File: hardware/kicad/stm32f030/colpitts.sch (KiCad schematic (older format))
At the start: 42 parts, among them P2 LOOP1, P3 LOOP2, Q1 BSS138, Q2 BC817-40, Q3 BSS138, Q4 BC817-40, T1 78601/9C, T2 78601/9C

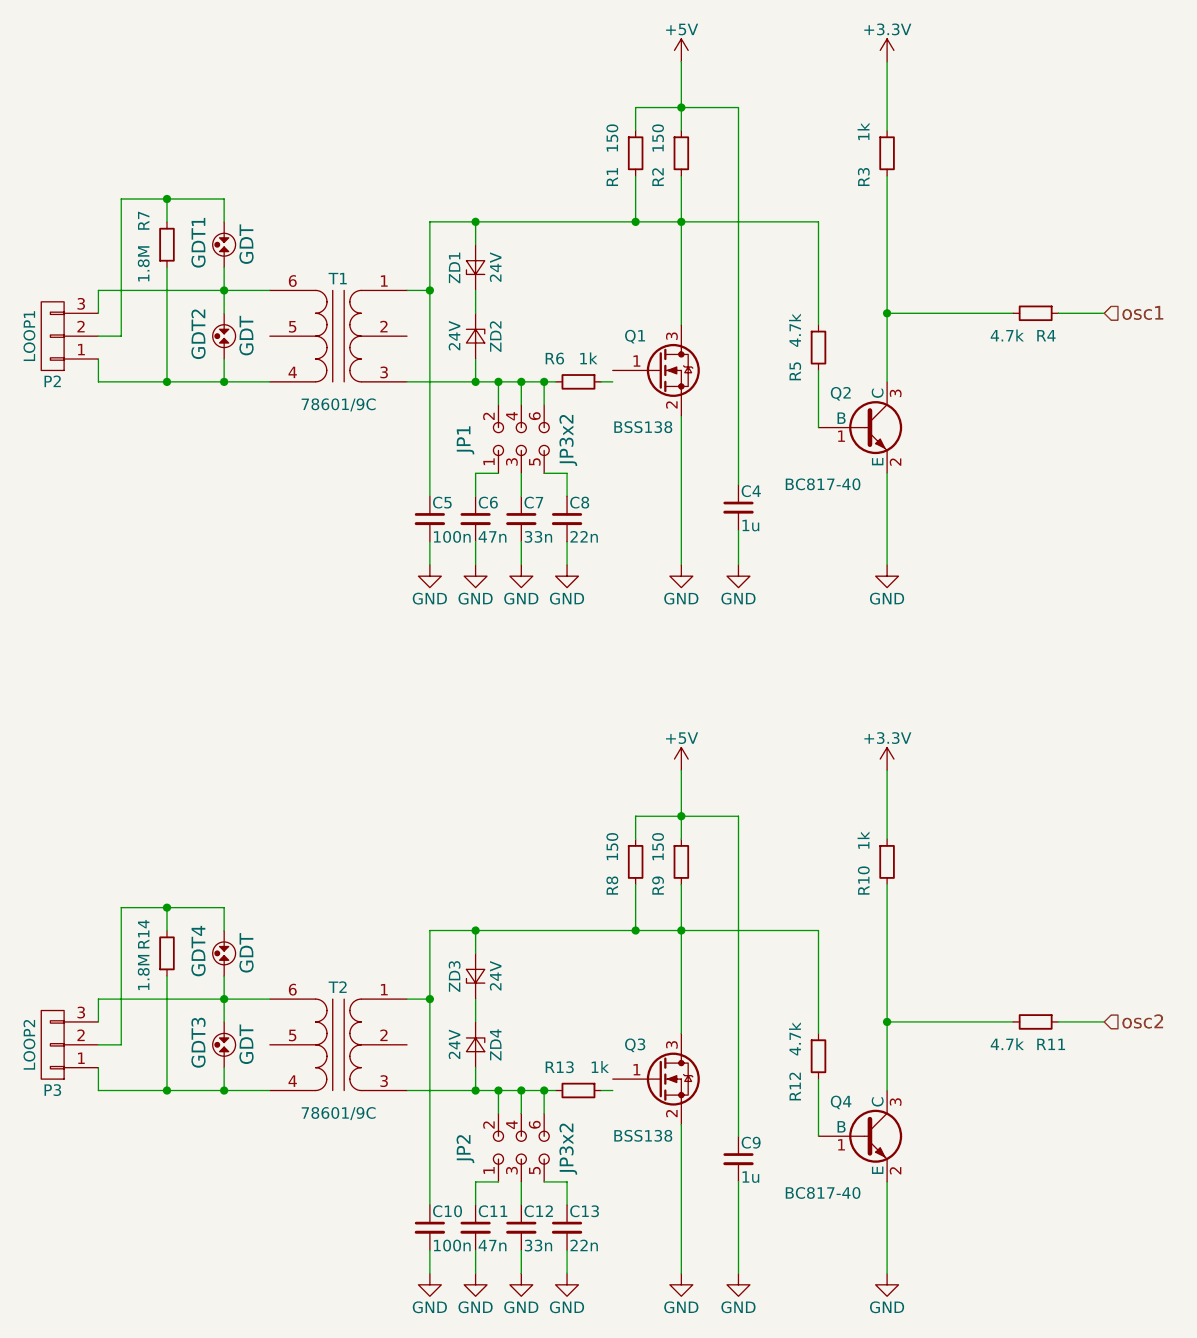
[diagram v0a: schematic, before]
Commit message: hardware/kicad/stm32f030: kicad version && lib bump
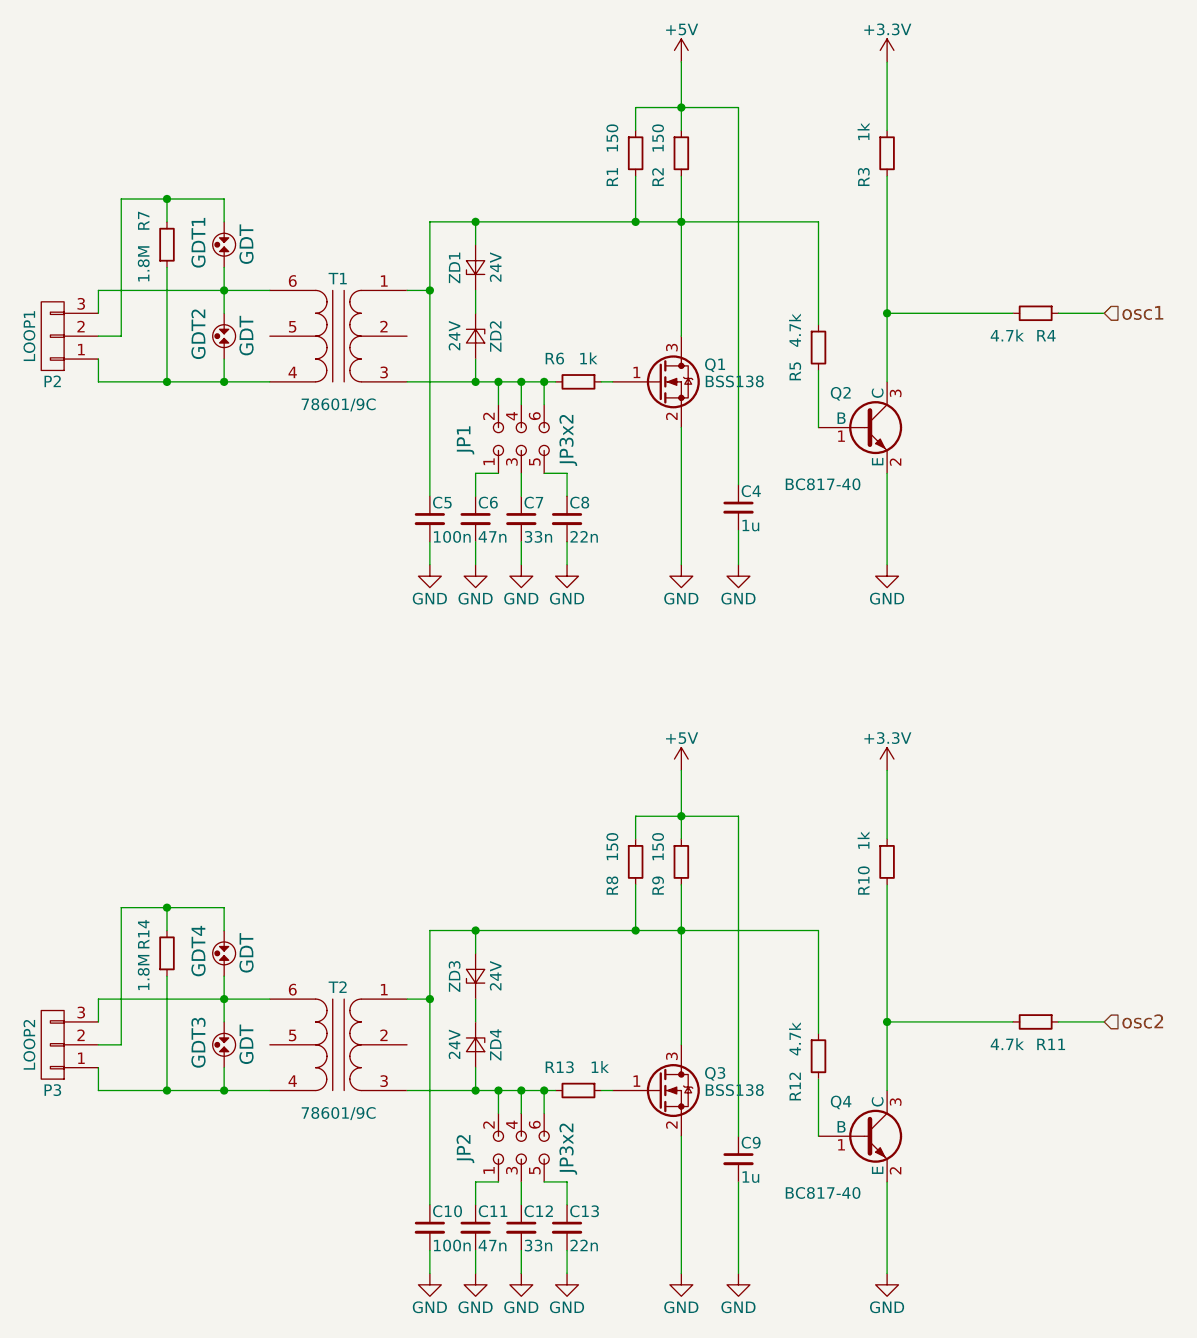
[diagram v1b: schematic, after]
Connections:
- net at R13.1: now also Q3.1 (G)
- net at R6.1: now also Q1.1 (G)
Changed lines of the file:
@@
 LIBS:transistors
 LIBS:conn
-LIBS:linear
 LIBS:regul
-LIBS:74xx
-LIBS:cmos4000
-LIBS:adc-dac
-LIBS:memory
-LIBS:xilinx
-LIBS:microcontrollers
-LIBS:dsp
-LIBS:microchip
-LIBS:analog_switches
-LIBS:motorola
-LIBS:texas
-LIBS:intel
-LIBS:audio
-LIBS:interface
-LIBS:digital-audio
-LIBS:philips
-LIBS:display
-LIBS:cypress
-LIBS:siliconi
-LIBS:opto
-LIBS:contrib
-LIBS:valves
 LIBS:stm32
 LIBS:switches
@@
 $EndComp
 $Comp
-L BSS138 Q3
-U 1 1 588475CA
-P 4000 5800
-F 0 "Q3" H 3850 5950 50  0000 L CNN
-F 1 "BSS138" H 3800 5550 50  0000 L CNN
-F 2 "TO_SOT_Packages_SMD:SOT-23" H 4200 5725 50  0001 L CIN
-F 3 "" H 4000 5800 50  0000 L CNN
-	1    4000 5800
-	1    0    0    -1
-$EndComp
-$Comp
 L GND #PWR012
 U 1 1 588475CB
@@
 $EndComp
 $Comp
-L BSS138 Q1
-U 1 1 5884A730
-P 4000 2700
-F 0 "Q1" H 3850 2850 50  0000 L CNN
-F 1 "BSS138" H 3800 2450 50  0000 L CNN
-F 2 "TO_SOT_Packages_SMD:SOT-23" H 4200 2625 50  0001 L CIN
-F 3 "" H 4000 2700 50  0000 L CNN
-	1    4000 2700
-	1    0    0    -1
-$EndComp
-$Comp
 L GND #PWR020
 U 1 1 5884A737
@@
 	3750 5850 3800 5850
 Wire Wire Line
-	4100 6650 4100 6000
+	4100 6650 4100 6050
 Wire Wire Line
 	3900 4750 3900 4650
@@
 	5000 4950 5000 5850
 Wire Wire Line
-	4100 4950 4100 5600
+	4100 4950 4100 5650
 Connection ~ 3200 5150
 Wire Wire Line
@@
 	3750 2750 3800 2750
 Wire Wire Line
-	4100 3550 4100 2900
+	4100 3550 4100 2950
 Wire Wire Line
 	3900 1650 3900 1550
@@
 	5000 1850 5000 2750
 Wire Wire Line
-	4100 1850 4100 2500
+	4100 1850 4100 2550
 Connection ~ 3200 2050
 Wire Wire Line
@@
 Wire Wire Line
 	1550 2750 2300 2750
+$Comp
+L BSS138 Q1
+U 1 1 59C1242F
+P 4000 2750
+F 0 "Q1" H 4200 2825 50  0000 L CNN
+F 1 "BSS138" H 4200 2750 50  0000 L CNN
+F 2 "TO_SOT_Packages_SMD:SOT-23" H 4200 2675 50  0001 L CIN
+F 3 "" H 4000 2750 50  0001 L CNN
+	1    4000 2750
+	1    0    0    -1
+$EndComp
+$Comp
+L BSS138 Q3
+U 1 1 59C12ACE
+P 4000 5850
+F 0 "Q3" H 4200 5925 50  0000 L CNN
+F 1 "BSS138" H 4200 5850 50  0000 L CNN
+F 2 "TO_SOT_Packages_SMD:SOT-23" H 4200 5775 50  0001 L CIN
+F 3 "" H 4000 5850 50  0001 L CNN
+	1    4000 5850
+	1    0    0    -1
+$EndComp
 $EndSCHEMATC

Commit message: kicad-STM32F030 modifications during test batch assembly
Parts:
- C10, C5: footprint Capacitors_SMD:C_0805_HandSoldering -> Capacitors_SMD:C_1206_HandSoldering
- C11, C6: footprint Capacitors_SMD:C_0805_HandSoldering -> Capacitors_SMD:C_1206
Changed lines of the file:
@@
 F 0 "C10" H 3010 6520 50  0000 L CNN
 F 1 "100n" H 3010 6370 50  0000 L CNN
-F 2 "Capacitors_SMD:C_0805_HandSoldering" H 3000 6450 50  0001 C CNN
+F 2 "Capacitors_SMD:C_1206_HandSoldering" H 3000 6450 50  0001 C CNN
 F 3 "" H 3000 6450 50  0000 C CNN
 	1    3000 6450
@@
 F 0 "C11" H 3210 6520 50  0000 L CNN
 F 1 "47n" H 3210 6370 50  0000 L CNN
-F 2 "Capacitors_SMD:C_0805_HandSoldering" H 3200 6450 50  0001 C CNN
+F 2 "Capacitors_SMD:C_1206" H 3200 6450 50  0001 C CNN
 F 3 "" H 3200 6450 50  0000 C CNN
 	1    3200 6450
@@
 F 0 "C5" H 3010 3420 50  0000 L CNN
 F 1 "100n" H 3010 3270 50  0000 L CNN
-F 2 "Capacitors_SMD:C_0805_HandSoldering" H 3000 3350 50  0001 C CNN
+F 2 "Capacitors_SMD:C_1206_HandSoldering" H 3000 3350 50  0001 C CNN
 F 3 "" H 3000 3350 50  0000 C CNN
 	1    3000 3350
@@
 F 0 "C6" H 3210 3420 50  0000 L CNN
 F 1 "47n" H 3210 3270 50  0000 L CNN
-F 2 "Capacitors_SMD:C_0805_HandSoldering" H 3200 3350 50  0001 C CNN
+F 2 "Capacitors_SMD:C_1206" H 3200 3350 50  0001 C CNN
 F 3 "" H 3200 3350 50  0000 C CNN
 	1    3200 3350
